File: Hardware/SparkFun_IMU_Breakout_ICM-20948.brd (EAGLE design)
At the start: 25.4 x 25.4 mm, 65 parts, among them U1 9DoF IMU, U2 TXB0108DQSR

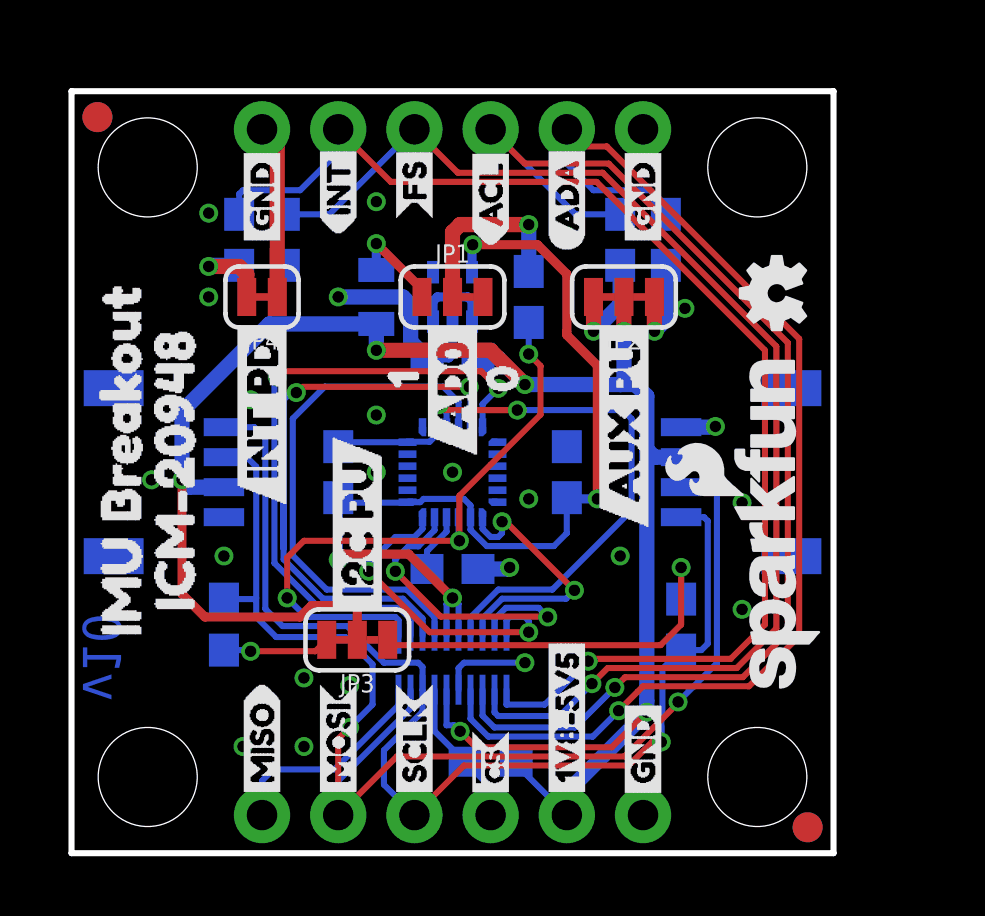
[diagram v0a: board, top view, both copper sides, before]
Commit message: Prettified the schematic
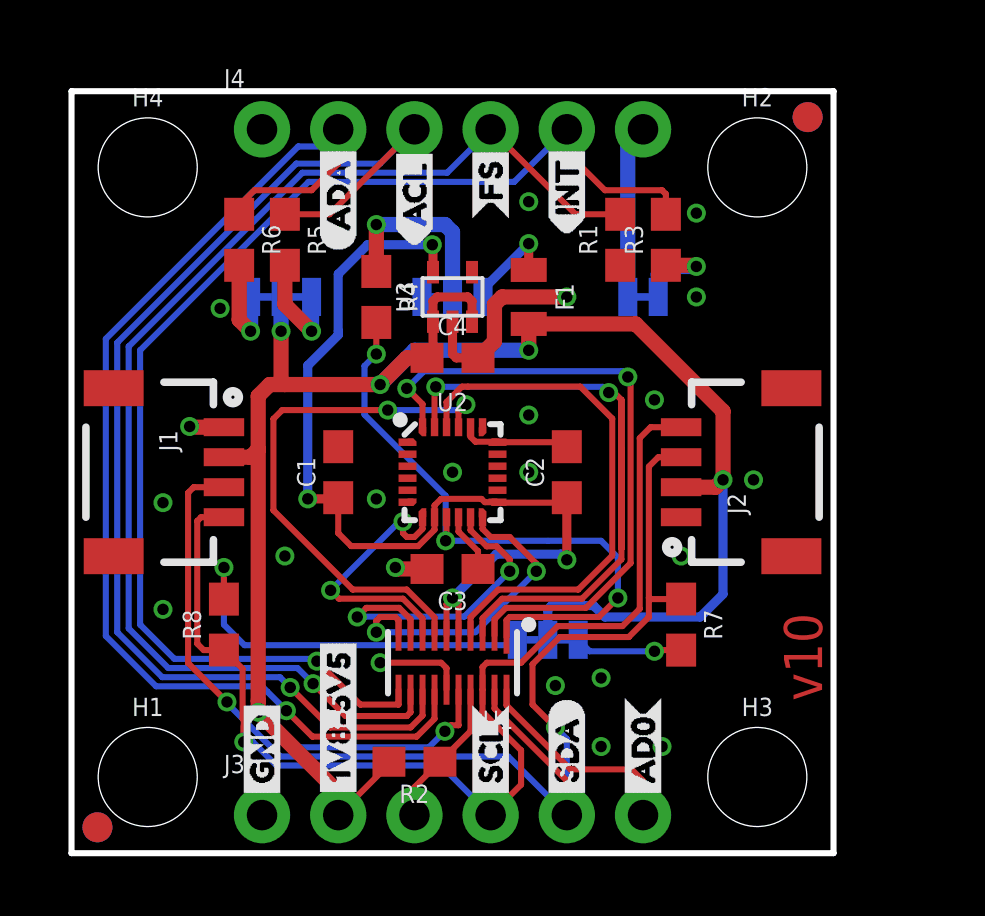
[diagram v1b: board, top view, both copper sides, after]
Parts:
- JP1: value AD0/SDO Pull -> INT PD; device SparkFun-Jumpers:SMT-JUMPER_3_1-NC_TRACE_SILK -> SparkFun-Jumpers:SMT-JUMPER_2_NC_TRACE_SILK
- JP2: value AUX -> AD0/SDO Pull; device SparkFun-Jumpers:SMT-JUMPER_3_2-NC_TRACE_SILK -> SparkFun-Jumpers:SMT-JUMPER_3_1-NC_TRACE_SILK
- JP3: value I2C PU -> AUX
- JP4: value INT PD -> I2C PU; device SparkFun-Jumpers:SMT-JUMPER_2_NC_TRACE_SILK -> SparkFun-Jumpers:SMT-JUMPER_3_2-NC_TRACE_SILK
- R4: value 2.2k -> 10k
- R8: value 10k -> 2.2k
- U1: value 9DoF IMU -> TXB0108DQSR; device SparkFun-Sensors:QFN24-3X3 -> SparkFun-IC-Comms:UFDFN-20
- U2: value TXB0108DQSR -> 9DoF IMU; device SparkFun-IC-Comms:UFDFN-20 -> SparkFun-Sensors:QFN24-3X3
- moved FRAME1 38.1 mm to (-6.35, -12.1), flipped to the top
- moved H3 28.7 mm to (22.9, 2.54), flipped to the top
- moved FD1 23.7 mm to (0.86, 0.86)
- moved FD2 23.7 mm to (24.5, 24.5), flipped to the bottom
- moved FD3 23.7 mm to (24.5, 24.5)
- moved FD4 23.7 mm to (0.86, 0.86), flipped to the top
- moved U$30 22.1 mm to (23.7, 6.10), flipped to the bottom
- moved LOGO1 21.6 mm to (1.91, 11.0), flipped to the bottom
- moved LOGO2 21.6 mm to (1.91, 18.7), flipped to the bottom
- moved H2 20.3 mm to (22.9, 22.9), flipped to the top
- moved H4 20.3 mm to (2.54, 22.9), flipped to the top
- moved U$31 18.5 mm to (22.0, 6.99), flipped to the bottom
- moved R5 18.4 mm to (7.11, 20.4), flipped to the top, turned to 270 degrees
- moved R1 17.9 mm to (18.3, 20.4), flipped to the top, turned to 90 degrees
- moved R2 16.0 mm to (11.4, 3.05), flipped to the top, turned to 180 degrees
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- renumbered U$1 to U3, U$2 to A1
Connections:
- net !CS: now also U1.4, U2.22; no longer U1.22, U2.4
- net !CS!_VIN: now also R2.1, U1.17; no longer R1.1, U2.17
- net 1.8V: now also C1.1, U1.5, U1.6, U2.13, U2.8; no longer C3.1, U1.13, U1.8, U2.5, U2.6
- net AD0/SDO: now also R4.2, U1.1, U2.9; no longer R2.2, U1.9, U2.1
- net AD0/SDO_VIN: now also U1.20; no longer U2.20
- net AUX_CL: now also U1.8, U2.7; no longer U1.7, U2.8
- net AUX_CL_VIN: now also R5.1, U1.13; no longer R6.1, U2.13
- net AUX_DA: now also U1.7, U2.21; no longer U1.21, U2.7
- net AUX_DA_VIN: now also R6.1, U1.14; no longer R7.1, U2.14
- net FSYNC: now also U1.9, U2.11; no longer U1.11, U2.9
- net FSYNC_VIN: now also R1.2, U1.12; no longer R3.2, U2.12
- net GND: now also JP1.1, JP2.3, R1.1, U1.15, U2.18, U2.20; no longer JP1.3, JP4.1, R3.1, U1.18, U1.20, U2.15
- net INT: now also U1.10, U2.12; no longer U1.12, U2.10
- net INT_VIN: now also R3.2, U1.11; no longer R8.2, U2.11
- net N$1: now also C3.1, U2.10; no longer C1.1, U1.10
- net N$2: now also JP2.1; no longer JP1.1
- net N$3: now also JP2.2, R4.1; no longer JP1.2, R2.1
- net N$4: now also JP4.3, R7.2; no longer JP3.3, R4.2
- net N$5: now also JP4.1, R8.2; no longer JP3.1, R5.2
- net N$6: now also JP3.3, R5.2; no longer JP2.3, R6.2
- net N$7: now also JP3.1, R6.2; no longer JP2.1, R7.2
- net N$8: now also JP1.2, R3.1; no longer JP4.2, R8.1
- net SCL/SCLK: now also U1.3, U2.23; no longer U1.23, U2.3
- net SCL/SCLK_VIN: now also R8.1, U1.18; no longer R5.1, U2.18
- net SDA/SDI: now also U1.2, U2.24; no longer U1.24, U2.2
- net SDA/SDI_VIN: now also R7.1, U1.19; no longer R4.1, U2.19
- net VIN: now also JP4.2, R2.2, U1.16; no longer JP2.2, R1.2, U2.16

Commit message: Push to work from laptop
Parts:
- removed F1: 6V 0.5A, SparkFun-Fuses:0805
- added D1: RED, SparkFun-LED:LED-0603
- added JP5: LED, SparkFun-Jumpers:SMT-JUMPER_2_NC_TRACE_SILK
- added R9: 470, SparkFun-Resistors:0603
- JP2: value AD0/SDO Pull -> AD0; device SparkFun-Jumpers:SMT-JUMPER_3_1-NC_TRACE_SILK -> SparkFun-Jumpers:SMT-JUMPER_2_NO_SILK
- moved JP2 18.9 mm to (27.8, 7.21), turned to 90 degrees
- moved R4 16.8 mm to (22.5, 7.11), turned to 90 degrees
- moved R2 9.32 mm to (3.05, 7.11), turned to 90 degrees
- moved FRAME1 8.98 mm to (2.54, -10.8)
- moved R7 0.51 mm to (20.3, 7.11)
- moved R8 0.51 mm to (5.08, 7.11)
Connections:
- removed net N$2: F1.1, JP2.1
- removed net N$3: JP2.2, R4.1
- new net N$10: JP5.2, R9.1
- new net N$9: D1.C, R9.2
- net 1.8V: now also D1.A
- net AD0/SDO: no longer R4.2
- net AD0/SDO_VIN: now also JP2.2, R4.1
- net GND: now also JP2.1, JP5.1; no longer JP2.3
- net VIN: now also R4.2; no longer F1.2
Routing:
- net !CS!_VIN: track 4.95 -> 15.7 mm, vias 0 -> 1
- net N$9: track 0.00 -> 7.05 mm
- net N$3: track 6.37 -> 0.00 mm, vias 1 -> 0
- net AD0/SDO_VIN: track 7.25 -> 13.1 mm
- net GND: track 21.2 -> 16.7 mm, vias 23 -> 25
- net INT: track 10.8 -> 15.2 mm
- net N$2: track 3.29 -> 0.00 mm, vias 1 -> 0
- net 1.8V: track 32.9 -> 35.5 mm
- net N$10: track 0.00 -> 2.10 mm, vias 0 -> 1
- net AUX_CL: track 8.92 -> 11.0 mm
- net FSYNC: track 10.9 -> 12.9 mm
- net INT_VIN: track 42.0 -> 40.6 mm
- net FSYNC_VIN: track 41.4 -> 40.0 mm
- net AUX_DA_VIN: track 39.4 -> 38.1 mm
- net AUX_CL_VIN: track 40.5 -> 39.1 mm
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
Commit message: 95% ready for review commit
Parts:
- added U$1: (no value), buzzard_labels (1):NC0
- moved JP2 6.23 mm to (21.7, 5.94)
- moved R1 0.89 mm to (18.3, 19.6)
- moved R3 0.89 mm to (19.8, 19.6)
- moved R5 0.89 mm to (7.11, 19.6)
- moved R6 0.89 mm to (5.59, 19.6)
- moved FD1 0.18 mm to (0.74, 0.74)
- moved FD4 0.18 mm to (0.74, 0.74)
- moved FD2 0.18 mm to (24.7, 24.7)
- moved FD3 0.18 mm to (24.7, 24.7)
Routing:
- net SCL/SCLK: track 27.3 -> 19.1 mm
- net INT: track 15.2 -> 11.0 mm
- net AD0/SDO_VIN: track 13.1 -> 16.7 mm, vias 0 -> 1
- net VIN: track 70.8 -> 73.5 mm, vias 6 -> 7
- net N$7: track 3.50 -> 2.61 mm
- net N$6: track 3.71 -> 2.82 mm
- net FSYNC: track 12.9 -> 12.0 mm
- net N$5: track 13.1 -> 12.5 mm

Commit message: Design review
Made all routing look as clean as possible
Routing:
- net VIN: track 73.5 -> 72.7 mm
- net GND: vias 25 -> 26

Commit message: Trace routing changes during design review
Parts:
- removed A1: QWIIC_BOARD_OUTLINENH, SparkX:QWIIC_BOARD_MOUNT_NOHOLES
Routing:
- net SDA/SDI_VIN: track 44.2 -> 42.7 mm
- net SCL/SCLK_VIN: track 38.0 -> 37.1 mm

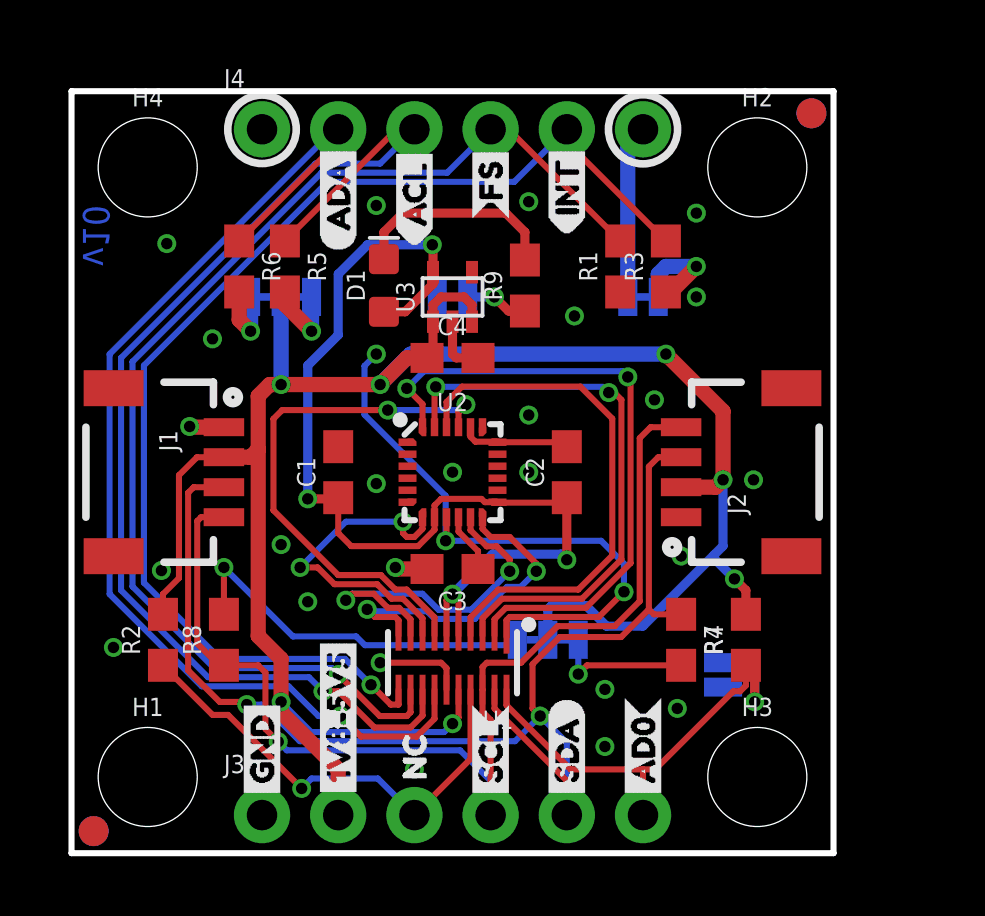
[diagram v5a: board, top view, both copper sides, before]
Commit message: Fixes notes from issue #1
In response to issue #1 I have:
- Replaced an existing 0.1 uF cap with 1.0 uF
- Changed address references to hex in .sch
- Questioned why we worry about vector font now that we use Buzzard
- Tried LED at 1.8V w and w/o CL resistor (1k). All is well
- Fixed all silk issues
- Research indicates that copper is not ferromagnetic (instead it is dimagnetic) so not a concern for the magnetometer
- Moved triple jumpers away from obstacles
- Slightly improved ground pour connectivity
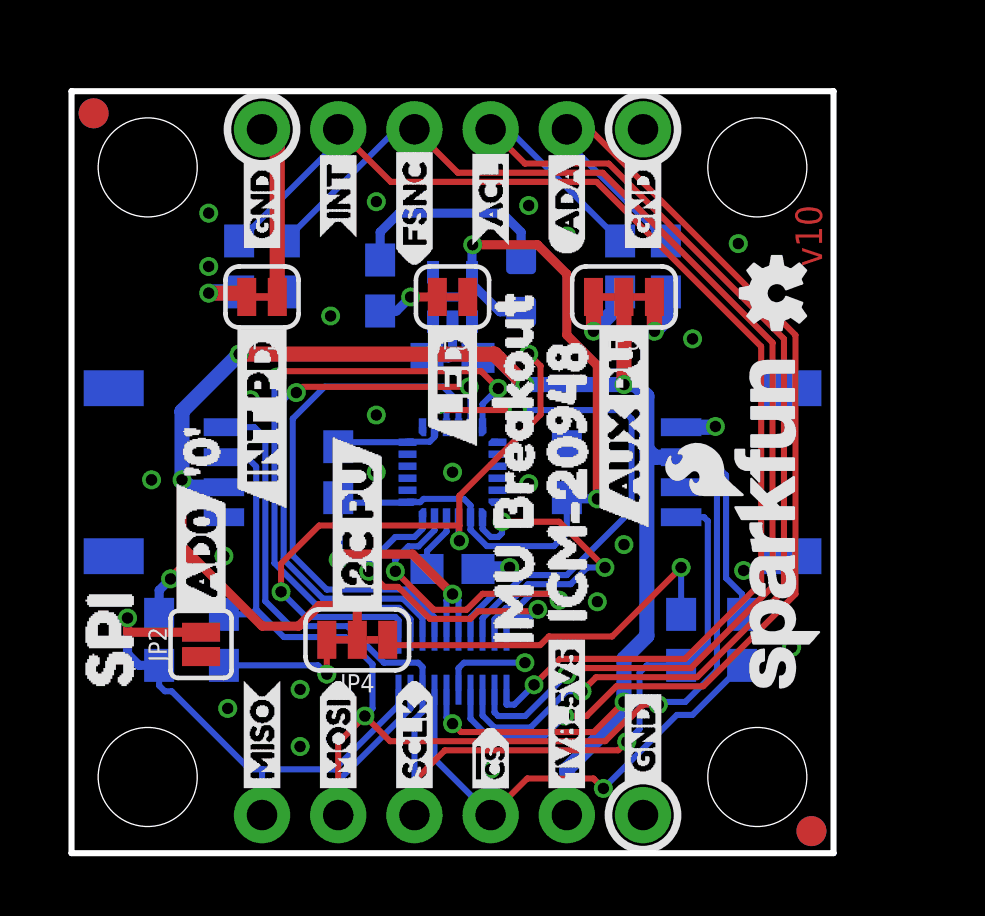
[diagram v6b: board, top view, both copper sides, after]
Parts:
- added U$2: (no value), buzzard_labels_2:GND4
- added U$32: (no value), buzzard_labels_2:#0#25
- C1: value 0.1uF -> 1.0uF
- U$1: device buzzard_labels (1):NC0 -> buzzard_labels_2:GND4
- U$10: device buzzard_labels:ACL9 -> buzzard_labels_2:SCLK15
- U$11: device buzzard_labels:ADA16 -> buzzard_labels_2:#CS16
- U$12: device buzzard_labels:FS15 -> buzzard_labels_2:1V8#5V57
- U$13: device buzzard_labels:INT8 -> buzzard_labels_2:VIN5
- U$14: device buzzard_labels:SCLK14 -> buzzard_labels_2:NC17
- U$15: device buzzard_labels:#CS13 -> buzzard_labels_2:SCL10
- U$16: device buzzard_labels:1V8#5V54 -> buzzard_labels_2:SDA11
- U$17: device buzzard_labels:GND2 -> buzzard_labels_2:AD012
- U$18: device buzzard_labels:INT8 -> buzzard_labels_2:ADA0
- U$19: device buzzard_labels:FS15 -> buzzard_labels_2:ACL1
- U$20: device buzzard_labels:ACL9 -> buzzard_labels_2:FSNC2
- U$21: device buzzard_labels:ADA16 -> buzzard_labels_2:INT3
- U$22: device buzzard_labels:GND2 -> buzzard_labels_2:GND4
- U$23: device buzzard_labels:GND2 -> buzzard_labels_2:I2C18
- U$24: device buzzard_labels:INT_PD17 -> buzzard_labels_2:AD020
- U$25: device buzzard_labels:AUX_PU15 -> buzzard_labels_2:I2C_PU21
- U$26: device buzzard_labels:AD014 -> buzzard_labels_2:SPI19
- U$27: device buzzard_labels:I2C_PU17 -> buzzard_labels_2:AUX_PU24
- U$28: device buzzard_labels:118 -> buzzard_labels_2:INT_PD24
- U$29: device buzzard_labels:019 -> buzzard_labels_2:LED23
- U$3: device buzzard_labels:MISO1 -> buzzard_labels_2:GND4
- U$4: device buzzard_labels:1V8#5V54 -> buzzard_labels_2:INT3
- U$5: device buzzard_labels:GND2 -> buzzard_labels_2:FSNC2
- U$6: device buzzard_labels:MOSI0 -> buzzard_labels_2:ACL1
- U$7: device buzzard_labels:SCL14 -> buzzard_labels_2:ADA0
- U$8: device buzzard_labels:SDA12 -> buzzard_labels_2:MISO13
- U$9: device buzzard_labels:AD010 -> buzzard_labels_2:MOSI14
- moved FD1 23.9 mm to (24.7, 0.74), flipped to the top
- moved FD2 23.9 mm to (0.74, 24.7), flipped to the top
- moved FD3 23.9 mm to (0.74, 24.7), flipped to the bottom
- moved FD4 23.9 mm to (24.7, 0.74), flipped to the bottom
- moved U$23 23.9 mm to (24.1, 4.06)
- moved U$3 22.2 mm to (6.35, 19.8), flipped to the top
- moved LOGO1 21.6 mm to (23.5, 11.0), flipped to the top
- moved LOGO2 21.6 mm to (23.5, 18.7), flipped to the top
- moved FRAME1 20.3 mm to (22.9, -10.8), flipped to the bottom
- moved H1 20.3 mm to (22.9, 2.54), flipped to the bottom
- moved H2 20.3 mm to (2.54, 22.9), flipped to the bottom
- moved H3 20.3 mm to (2.54, 2.54), flipped to the bottom
- moved H4 20.3 mm to (22.9, 22.9), flipped to the bottom
- moved R4 19.6 mm to (2.92, 7.11), flipped to the bottom
- moved U$12 19.5 mm to (16.5, 1.78)
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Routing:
- net AD0/SDO_VIN: track 16.3 -> 18.1 mm
- net N$8: track 3.51 -> 2.43 mm

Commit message: Add PWR LED and axes labels
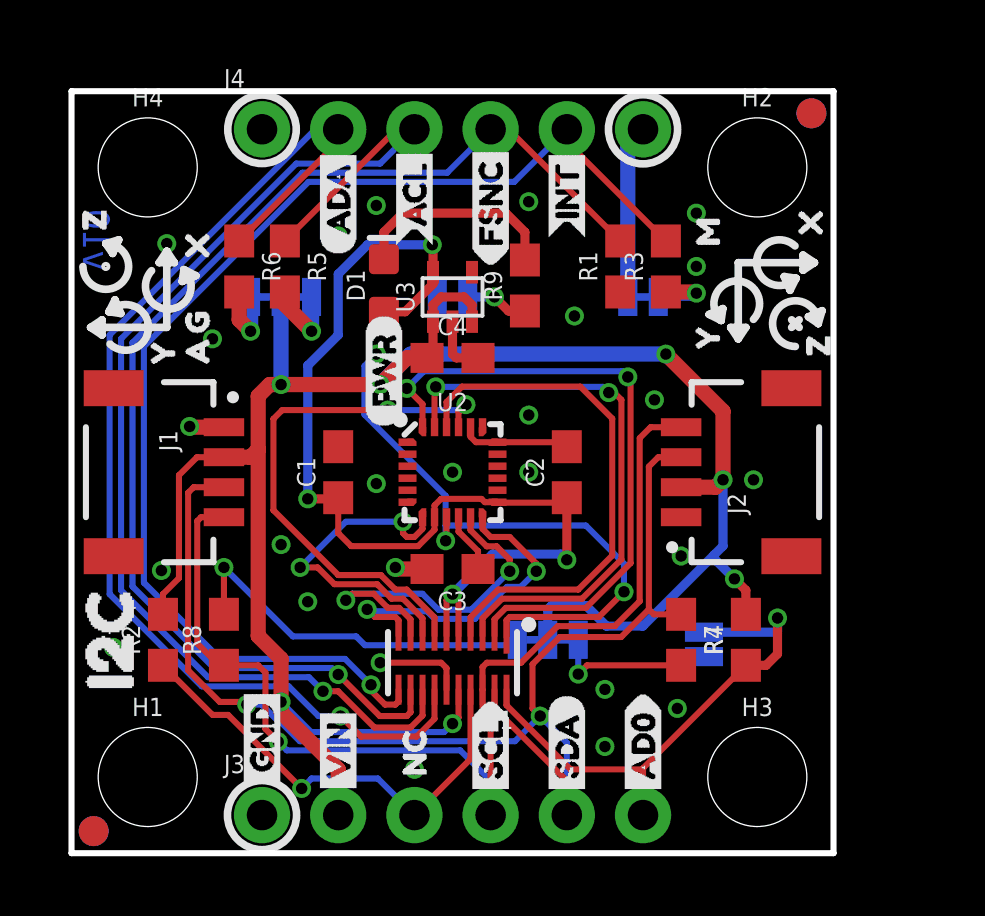
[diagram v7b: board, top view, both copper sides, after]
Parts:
- added U$33: (no value), buzzard_labels (1):PWR0
- added U$34, U$40: (no value), buzzard_labels (1):X0
- added U$35, U$41: (no value), buzzard_labels (1):Y1
- added U$36, U$42: (no value), buzzard_labels (1):Z2
- added U$37: (no value), buzzard_labels (1):G5
- added U$38: (no value), buzzard_labels (1):A4
- added U$39: (no value), buzzard_labels (1):M3
- J1, J2: device SparkFun-Connectors:1X04_1MM_RA -> SparkFun-Connectors:JST04_1MM_RA
- moved FD1 23.9 mm to (0.74, 0.74), flipped to the bottom
- moved FD2 23.9 mm to (24.7, 24.7), flipped to the bottom
- moved FD3 23.9 mm to (24.7, 24.7), flipped to the top
- moved FD4 23.9 mm to (0.74, 0.74), flipped to the top
- moved U$23 22.9 mm to (1.27, 4.06), flipped to the top
- moved U$26 22.9 mm to (24.1, 4.19), flipped to the bottom
- moved LOGO1 21.6 mm to (1.91, 11.0), flipped to the bottom
- moved LOGO2 21.6 mm to (1.91, 18.7), flipped to the bottom
- moved FRAME1 20.3 mm to (2.54, -10.8), flipped to the top
- moved H1 20.3 mm to (2.54, 2.54), flipped to the top
- moved H2 20.3 mm to (22.9, 22.9), flipped to the top
- moved H3 20.3 mm to (22.9, 2.54), flipped to the top
- moved H4 20.3 mm to (2.54, 22.9), flipped to the top
- moved R4 19.6 mm to (22.5, 7.11), flipped to the top
- moved R2 19.3 mm to (3.05, 7.11), flipped to the top
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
